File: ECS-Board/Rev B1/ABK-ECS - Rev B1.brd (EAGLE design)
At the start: 100 x 100 mm, 298 parts, among them J1 USB-B-S-RA, J10 FTSH-105-01-L-DV-NOPASTE, J11 22-05-7028-02, J12 RB1-125BAG1A, J13 22-05-7068-06, J14 22-05-7048-04, J15 22-05-7048-04, J16 22-05-7048-04, J2 MSTBA2, J3 22-05-7068-06, J5 22-05-7068-06, J6 22-05-7068-06, J7 22-05-7068-06, J8 22-05-7028-02, J9 FTSH-103-01-L-DV-NOPASTE, SW1 B3FS-1015, SW2 B3FS-1015, T1 MMBT2907ALT3, T10 MMBT2222AL, T11 IRLML5103TRPBF, T12 MMBT2222AL, T13 IRLML5103TRPBF, T14 IRLML5103TRPBF, T15 IRLML5103TRPBF, T16 IRLML5103TRPBF, T17 MMBT2222AL, T18 MMBT2222AL, T19 MMBT2222AL, T2 EXMACHINA-LOGO-NAME, T20 MMBT2222AL, T3 IRLML5103TRPBF, T4 IRLML5103TRPBF, T5 IRLML5103TRPBF, T6 IRLML5103TRPBF, T7 MMBT2222AL, T8 MMBT2222AL, T9 MMBT2222AL, U1 AT24C512C-SSHM-B, U10 SN74LVC2G17DBVR, U2 LPC1768FBD100, U3 LT3686HDDPBF, U4 LT3686HDDPBF, U5 CD4050BD, U6 CD4050BD, U7 DP83848JSQ/NOPB, U9 SN74LVC2G17DBVR, X1 FC-135, X2 ASE-12, X3 3000, X4 ASE_50

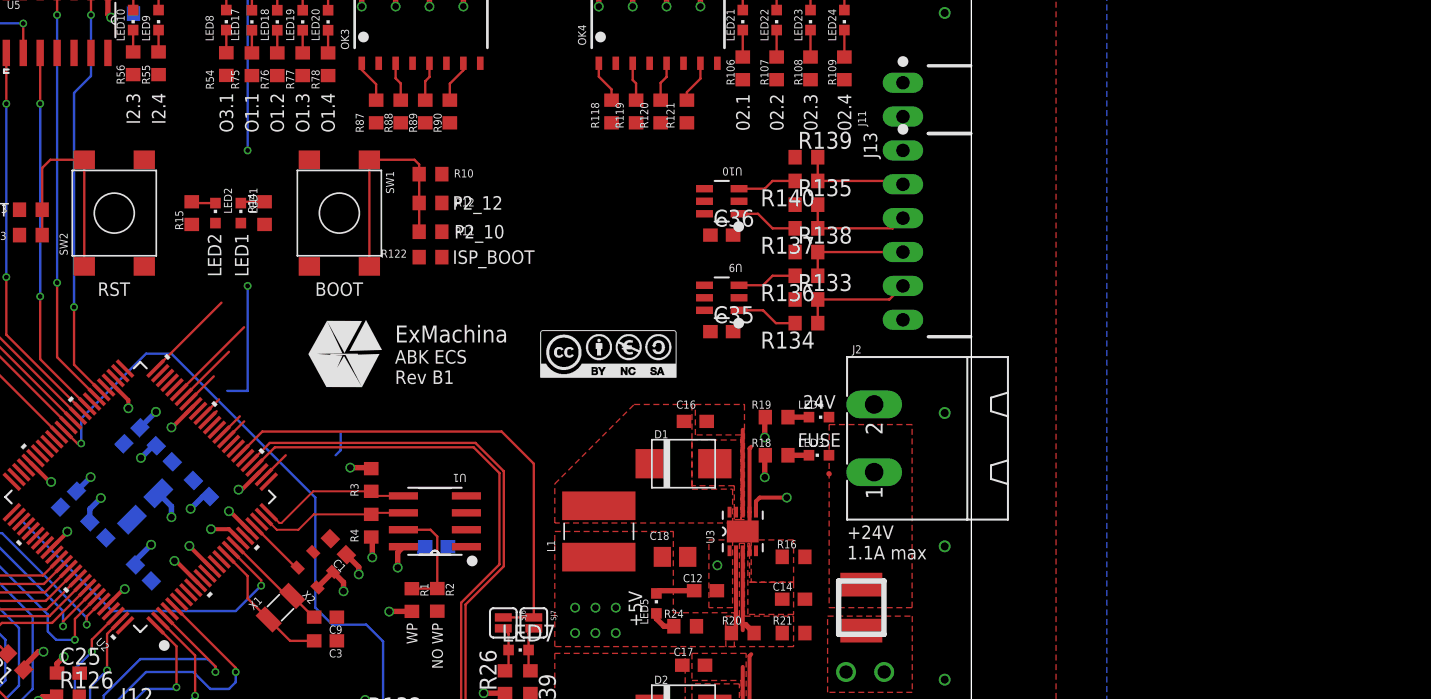
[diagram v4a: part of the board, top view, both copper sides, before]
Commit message: Route Outputs and Encoder Inputs
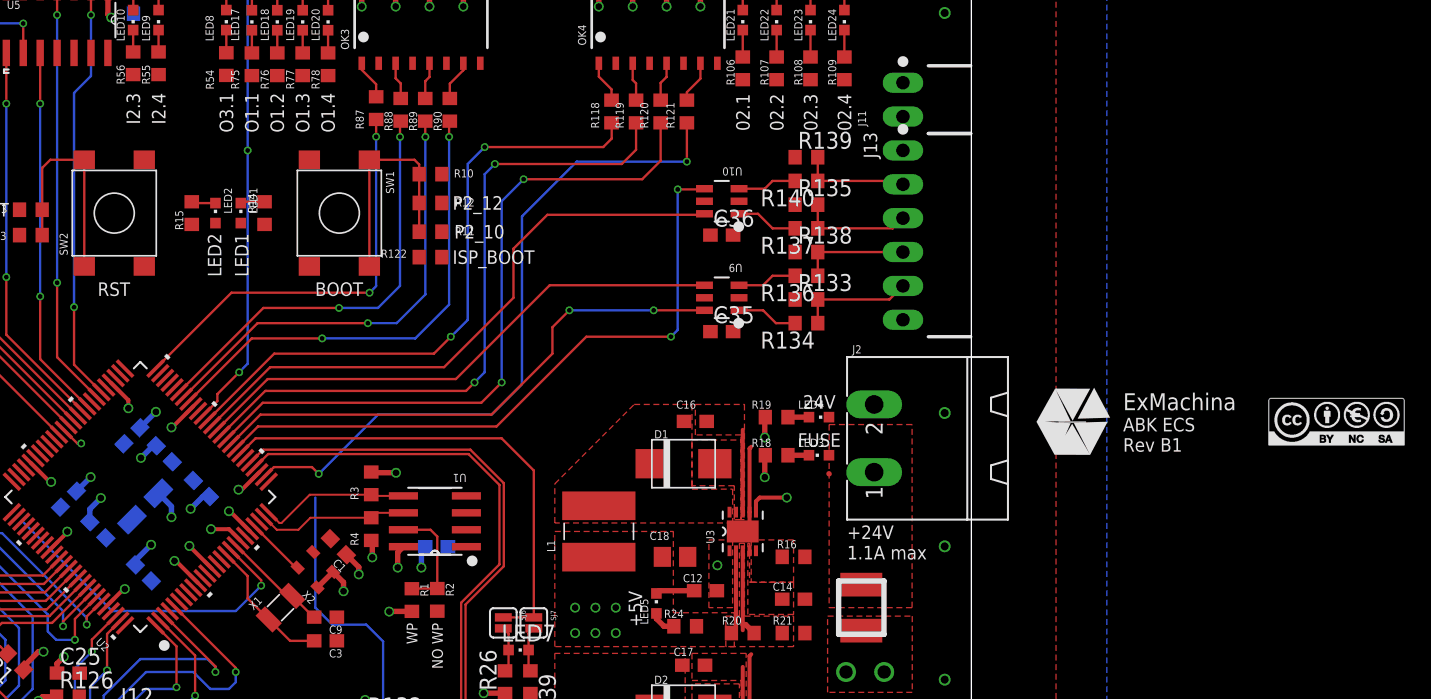
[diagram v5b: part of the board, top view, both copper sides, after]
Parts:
- moved CC1 54.8 mm to (127.4, 39.3)
- moved T2 54.8 mm to (107.6, 39.3)
- moved R87 0.25 mm to (55.4, 62.9)
- moved R4 0.25 mm to (55.0, 31.3)
- moved R3 0.25 mm to (55.0, 34.7)
- moved R88 0.13 mm to (57.2, 62.7)
- moved R89 0.13 mm to (59.0, 62.7)
- moved R90 0.13 mm to (60.9, 62.7)
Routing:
- net OUTPUT2.3_MCU: track 1.90 -> 52.0 mm, vias 0 -> 2
- net ENCODER_PUSH: track 0.00 -> 49.4 mm, vias 0 -> 2
- net OUTPUT2.2_MCU: track 1.94 -> 50.7 mm, vias 0 -> 2
- net OUTPUT2.4_MCU: track 4.24 -> 52.2 mm, vias 0 -> 2
- net OUTPUT2.1_MCU: track 0.98 -> 47.1 mm, vias 0 -> 2
- net ENCODER_Z: track 0.00 -> 45.6 mm
- net ENCODER_B: track 0.00 -> 41.1 mm
- net ENCODER_A: track 0.00 -> 40.8 mm, vias 0 -> 2
- net OUTPUT1.4_MCU: track 2.68 -> 36.3 mm, vias 0 -> 2
- net OUTPUT1.3_MCU: track 4.78 -> 34.3 mm, vias 0 -> 2
- net USB_CONNECT: track 55.5 -> 29.6 mm
- net OUTPUT1.2_MCU: track 6.88 -> 32.2 mm, vias 0 -> 2
- net OUTPUT1.1_MCU: track 6.99 -> 31.6 mm, vias 0 -> 2
- net OUTPUT3.2_MCU: track 38.9 -> 49.1 mm
- net +3V3: track 102.4 -> 103.6 mm, vias 45 -> 46
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
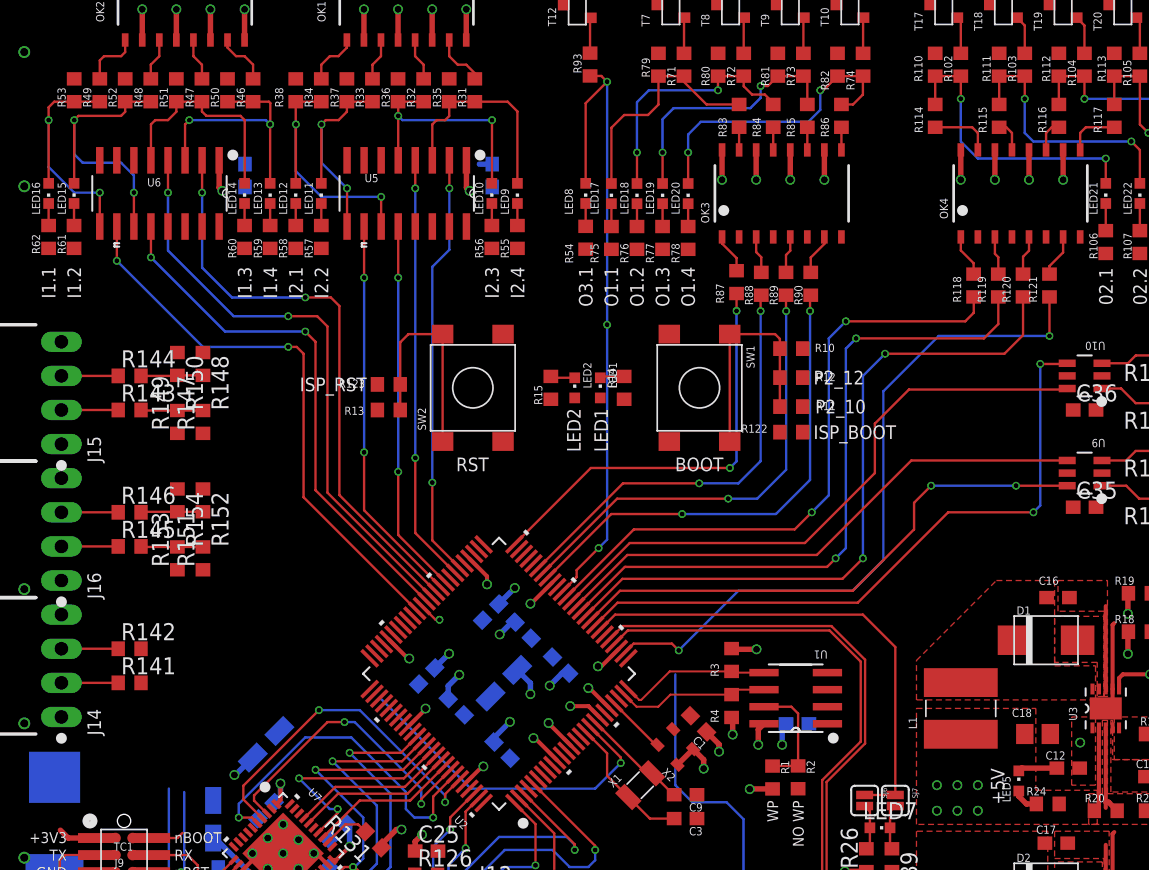
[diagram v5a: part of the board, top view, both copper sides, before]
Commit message: Route UART and I2C
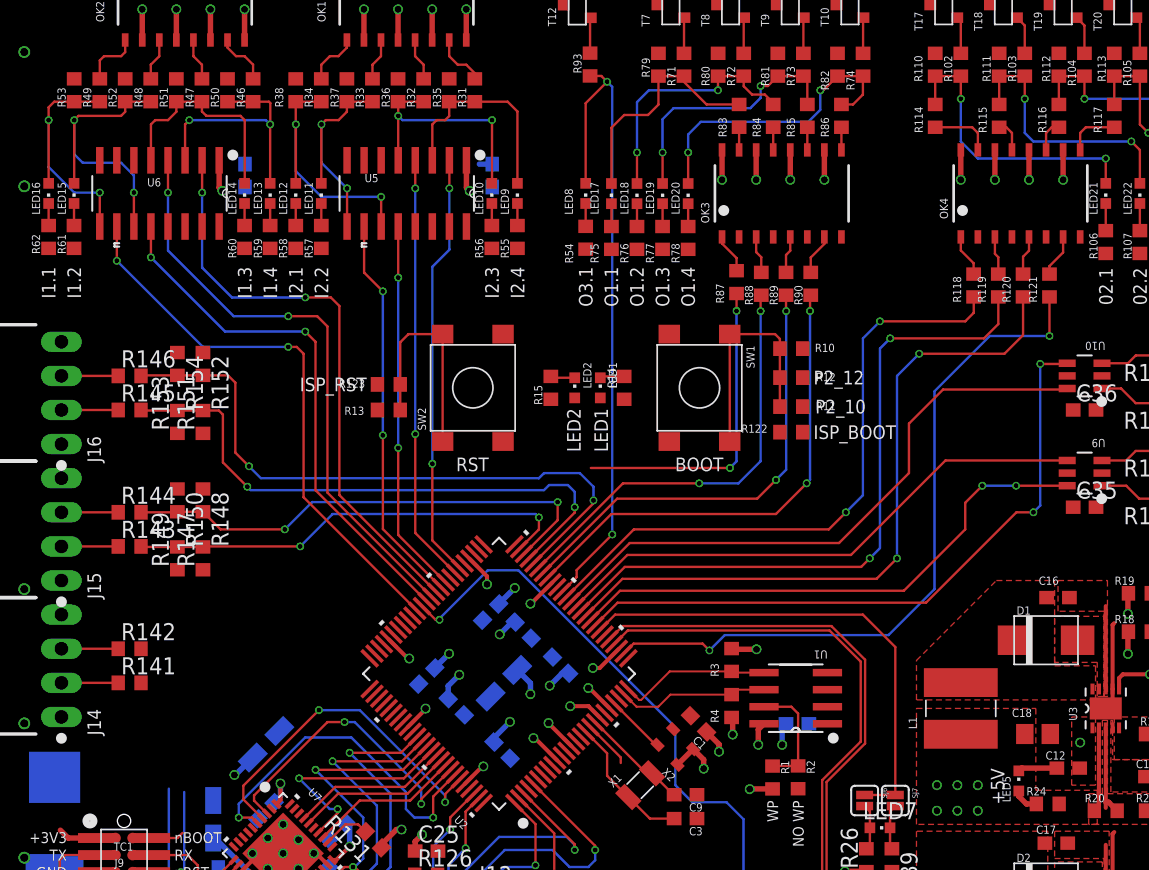
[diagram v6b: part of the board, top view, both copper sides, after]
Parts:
- moved R143 10.2 mm to (10.2, 43.2)
- moved R144 10.2 mm to (10.2, 45.7)
- moved R145 10.2 mm to (10.2, 53.3)
- moved R146 10.2 mm to (10.2, 55.9)
- moved R147 10.2 mm to (15.6, 42.3)
- moved R149 10.2 mm to (13.7, 42.3)
- moved R151 10.2 mm to (15.6, 52.5)
- moved R153 10.2 mm to (13.7, 52.5)
- moved J15 10.2 mm to (5.08, 44.5)
- moved J16 10.2 mm to (5.08, 54.6)
- moved R148 10.2 mm to (15.6, 46.6)
- moved R150 10.2 mm to (13.7, 46.6)
- moved R152 10.2 mm to (15.6, 56.8)
- moved R154 10.2 mm to (13.7, 56.8)
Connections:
- net I2C_SCL: now also R143.2, R147.2, R149.2; no longer R144.2, R148.2, R150.2
- net I2C_SDA: now also R144.2, R148.2, R150.2; no longer R143.2, R147.2, R149.2
- net UART_RX: now also R145.2, R151.2, R153.2; no longer R146.2, R152.2, R154.2
- net UART_TX: now also R146.2, R152.2, R154.2; no longer R145.2, R151.2, R153.2
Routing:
- net UART_TX: track 4.63 -> 48.1 mm, vias 0 -> 2
- net UART_RX: track 4.63 -> 43.6 mm, vias 0 -> 2
- net I2C_SDA: track 4.63 -> 37.3 mm, vias 0 -> 2
- net I2C_SCL: track 4.63 -> 33.7 mm, vias 0 -> 2
- net !RESET: track 63.8 -> 42.3 mm, vias 2 -> 1
- net USB_CONNECT: track 29.6 -> 49.7 mm
- net OUTPUT1.1_MCU: track 31.6 -> 23.6 mm
- net OUTPUT2.4_MCU: track 52.2 -> 53.5 mm
- net OUTPUT3.2_MCU: track 49.1 -> 49.4 mm, vias 3 -> 2

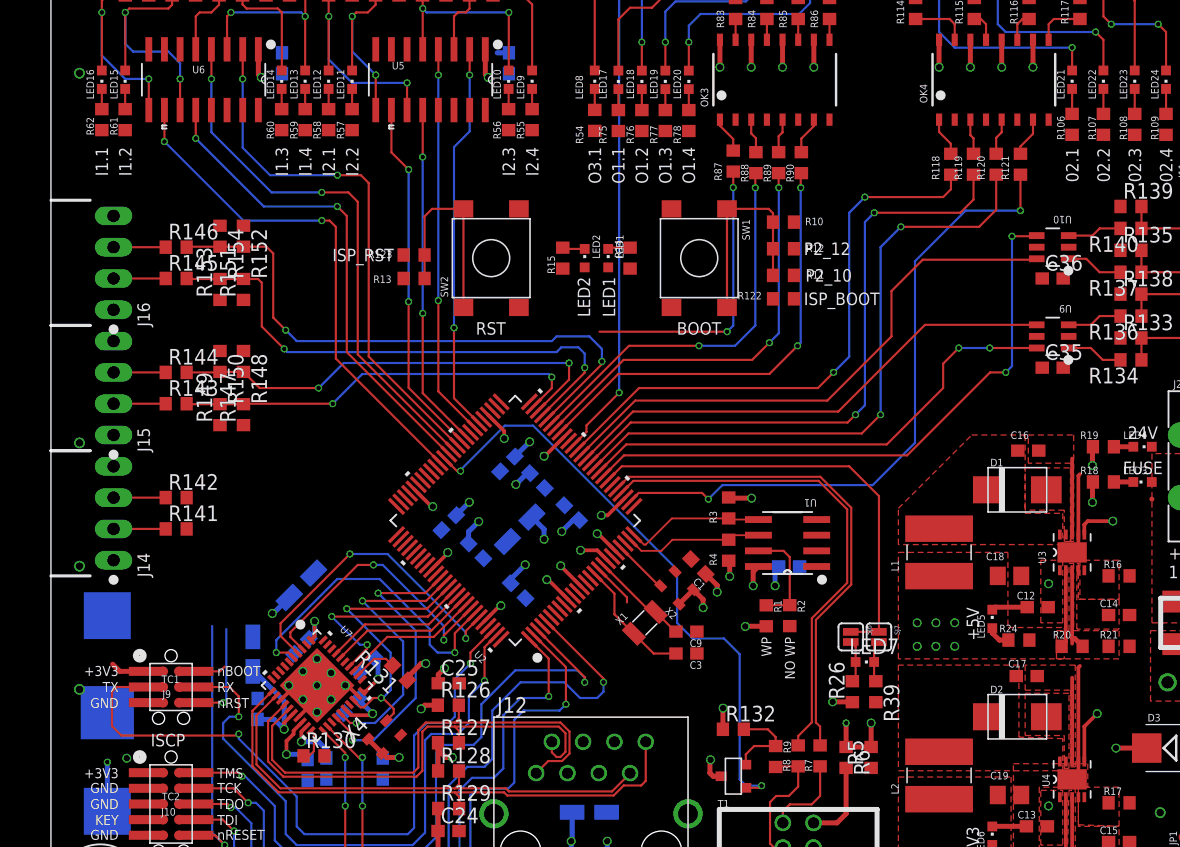
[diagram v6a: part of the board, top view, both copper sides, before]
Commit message: Route ADC
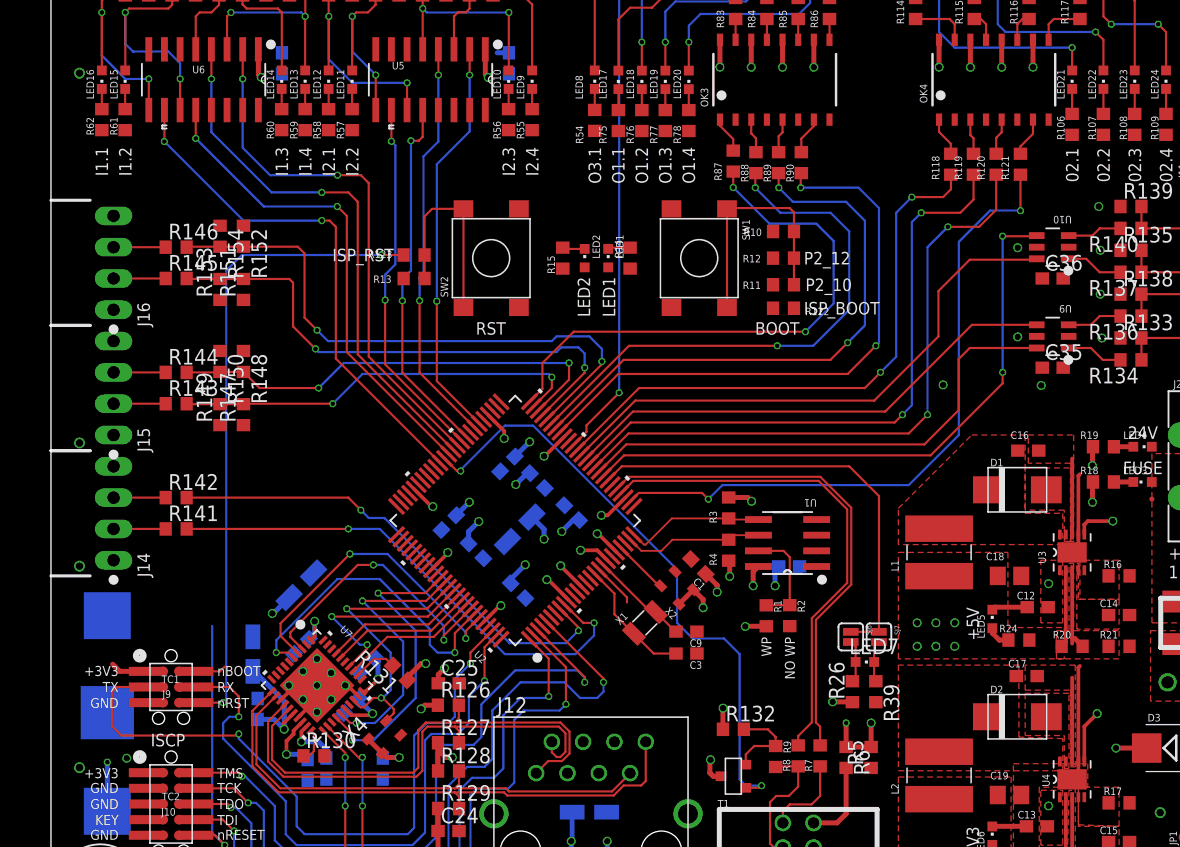
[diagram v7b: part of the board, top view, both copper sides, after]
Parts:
- moved R10 0.76 mm to (59.4, 57.1), turned to 180 degrees
- moved R11 0.76 mm to (59.4, 52.8), turned to 0 degrees
- moved R12 0.76 mm to (59.4, 55.0), turned to 0 degrees
- moved R122 0.76 mm to (59.4, 50.9), turned to 0 degrees
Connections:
- net ADC1: now also R142.2; no longer R141.2
- net ADC2: now also R141.2; no longer R142.2
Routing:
- net !ISP_RST: track 9.66 -> 53.7 mm, vias 1 -> 2
- net ADC2: track 0.00 -> 42.0 mm, vias 0 -> 2
- net ADC1: track 0.00 -> 39.5 mm, vias 0 -> 2
- net OUTPUT1.1_MCU: track 23.6 -> 45.5 mm
- net OUTPUT1.2_MCU: track 32.2 -> 44.7 mm
- net OUTPUT1.3_MCU: track 34.3 -> 46.3 mm
- net OUTPUT1.4_MCU: track 36.3 -> 48.1 mm
- net N$5: track 16.9 -> 19.5 mm
- net INPUT2.1_MCU: track 28.0 -> 29.7 mm
- net ENCODER_A: track 40.8 -> 42.1 mm, vias 2 -> 0
- net INPUT2.3_MCU: track 32.0 -> 33.2 mm
- net INPUT2.4_MCU: track 31.7 -> 32.9 mm
- net ENCODER_PUSH: track 49.4 -> 50.2 mm
- net INPUT2.2_MCU: track 29.2 -> 29.9 mm
- net OUTPUT2.4_MCU: track 53.5 -> 54.0 mm
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
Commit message: Route the output
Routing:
- net +3V3: track 104.3 -> 121.3 mm, vias 49 -> 56
- net OUTPUT1.1: track 5.62 -> 16.9 mm
- net OUTPUT1.4: track 3.69 -> 13.9 mm
- net OUTPUT1.3: track 3.67 -> 13.1 mm
- net OUTPUT1.2: track 5.93 -> 12.9 mm
- net OUTPUT2.4: track 11.8 -> 18.4 mm
- net +5V: track 42.4 -> 49.0 mm
- net OUTPUT2.3: track 9.06 -> 13.8 mm
- net OUTPUT2.1: track 8.60 -> 12.1 mm
- net OUTPUT2.2: track 8.26 -> 11.6 mm
